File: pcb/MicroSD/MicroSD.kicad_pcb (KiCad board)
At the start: 2 copper layers, 30 x 40 mm, 15 parts, among them J1 Micro_SD_Card, J2 Conn_01x06_MountingPin, U2 AMS1117, U3 74LVC125

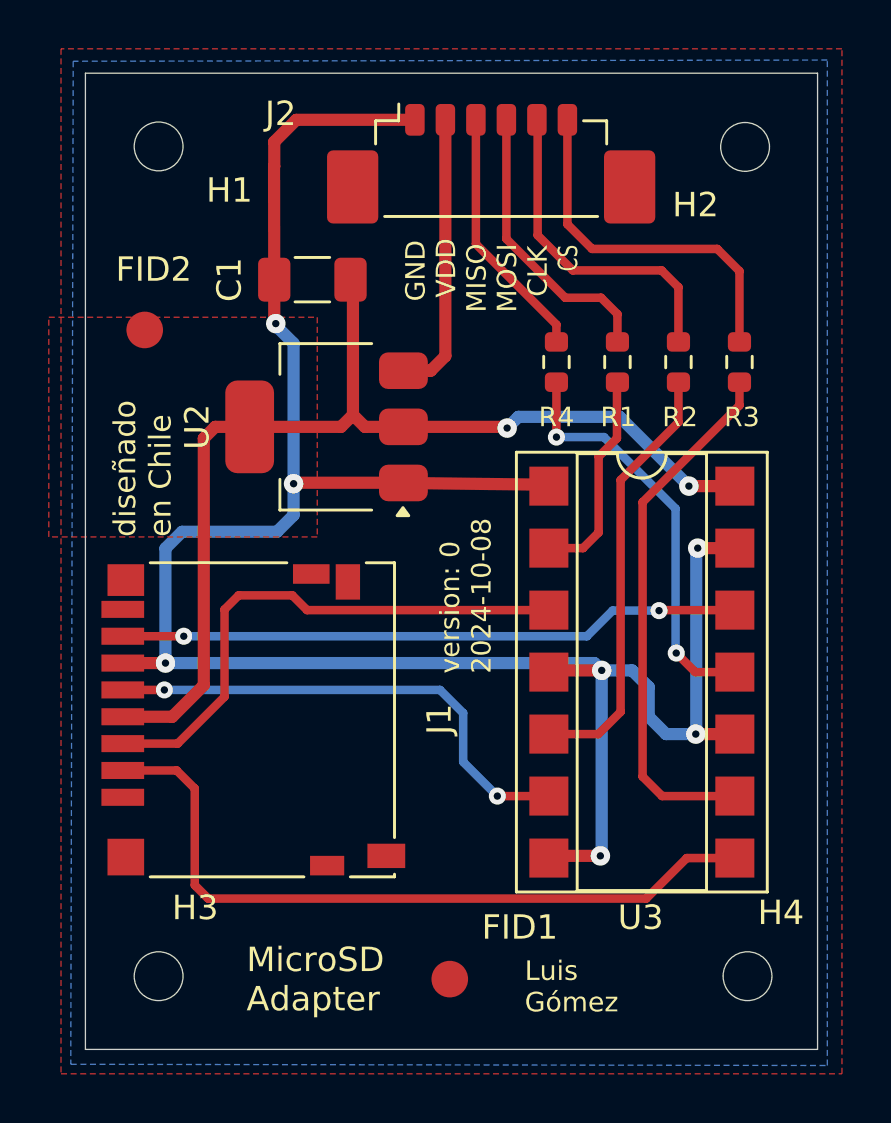
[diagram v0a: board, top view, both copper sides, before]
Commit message: se eliminan error del pcb
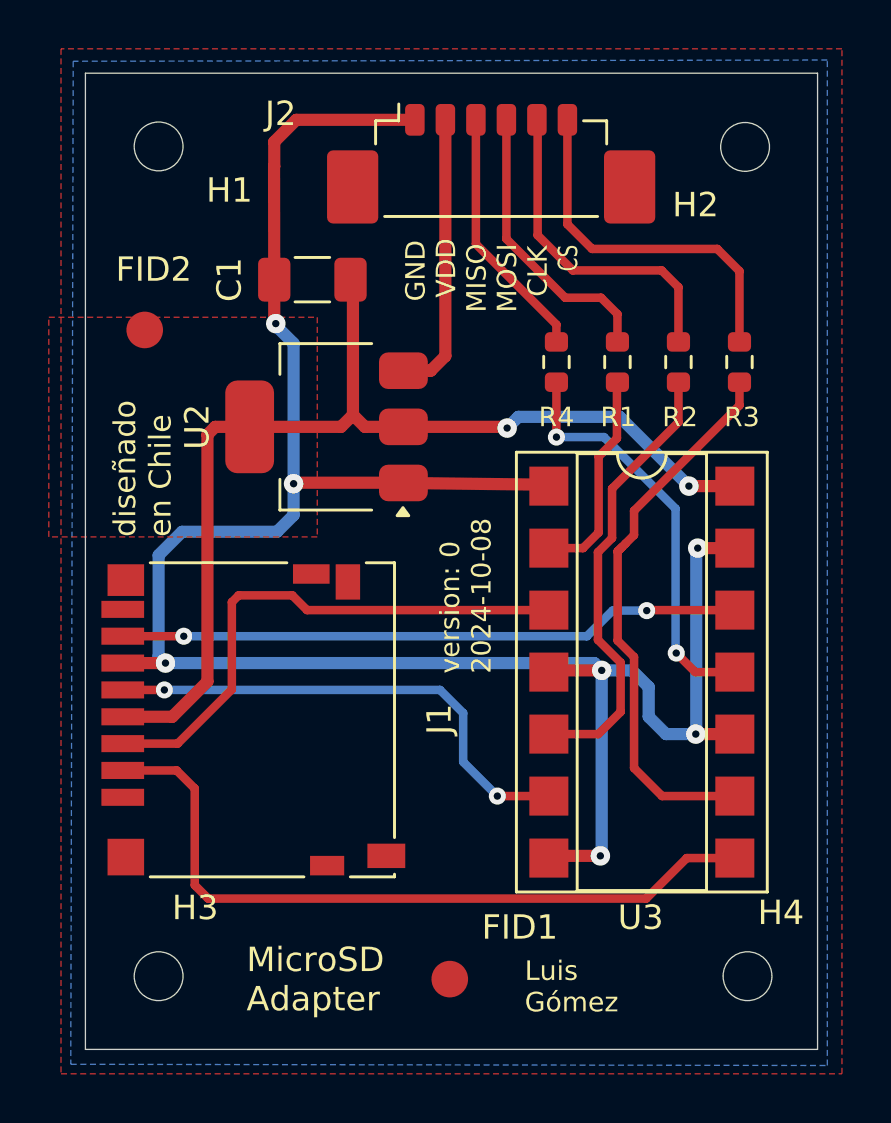
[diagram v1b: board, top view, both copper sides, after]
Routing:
- net Net-(R3-Pad2): track 21.9 -> 23.0 mm
- net Net-(R2-Pad2): track 17.8 -> 18.6 mm
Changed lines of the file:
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@@
+	)
+	(segment
+		(start 103.96 118.79)
+		(end 103 119.75)
+		(width 0.5)
+		(layer "B.Cu")
+		(net 1)
 	)
 	(segment
@@
 	)
 	(segment
+		(start 103 119.75)
+		(end 103 123.89)
+		(width 0.5)
+		(layer "B.Cu")
+		(net 1)
+	)
+	(segment
+		(start 125.01 127.08)
+		(end 123.79 127.08)
+		(width 0.5)
+		(layer "B.Cu")
+		(net 1)
+	)
+	(segment
+		(start 107.8 110.34)
+		(end 107.8 110.26)
+		(width 0.5)
+		(layer "B.Cu")
+		(net 1)
+	)
+	(segment
+		(start 107.85 118.79)
+		(end 103.96 118.79)
+		(width 0.5)
+		(layer "B.Cu")
+		(net 1)
+	)
+	(segment
+		(start 125.01 127.08)
+		(end 125.03 127.06)
+		(width 0.5)
+		(layer "B.Cu")
+		(net 1)
+	)
+	(segment
+		(start 125.03 119.52)
+		(end 125.09 119.46)
+		(width 0.5)
+		(layer "B.Cu")
+		(net 1)
+	)
+	(segment
+		(start 121.155 132.015)
+		(end 121.155 124.47)
+		(width 0.5)
+		(layer "B.Cu")
+		(net 1)
+	)
+	(segment
+		(start 123.08 125.15)
+		(end 122.4 124.47)
+		(width 0.5)
+		(layer "B.Cu")
+		(net 1)
+	)
+	(segment
+		(start 103 123.89)
+		(end 103.28 124.17)
+		(width 0.5)
+		(layer "B.Cu")
+		(net 1)
+	)
+	(segment
+		(start 108.53 111.07)
+		(end 107.8 110.34)
+		(width 0.5)
+		(layer "B.Cu")
+		(net 1)
+	)
+	(segment
 		(start 108.53 118.11)
 		(end 107.85 118.79)
@@
 	)
 	(segment
-		(start 125.01 127.08)
-		(end 123.79 127.08)
-		(width 0.5)
-		(layer "B.Cu")
-		(net 1)
-	)
-	(segment
-		(start 107.8 110.34)
-		(end 107.8 110.26)
-		(width 0.5)
-		(layer "B.Cu")
-		(net 1)
-	)
-	(segment
-		(start 125.01 127.08)
-		(end 125.03 127.06)
-		(width 0.5)
-		(layer "B.Cu")
-		(net 1)
-	)
-	(segment
-		(start 103.96 118.79)
-		(end 103.28 119.47)
-		(width 0.5)
-		(layer "B.Cu")
-		(net 1)
-	)
-	(segment
-		(start 125.03 119.52)
-		(end 125.09 119.46)
-		(width 0.5)
-		(layer "B.Cu")
-		(net 1)
-	)
-	(segment
-		(start 121.155 132.015)
-		(end 121.155 124.47)
-		(width 0.5)
-		(layer "B.Cu")
-		(net 1)
-	)
-	(segment
-		(start 123.08 125.15)
-		(end 122.4 124.47)
-		(width 0.5)
-		(layer "B.Cu")
-		(net 1)
-	)
-	(segment
 		(start 108.53 116.82)
 		(end 108.53 118.11)
-		(width 0.5)
-		(layer "B.Cu")
-		(net 1)
-	)
-	(segment
-		(start 108.53 111.07)
-		(end 107.8 110.34)
-		(width 0.5)
-		(layer "B.Cu")
-		(net 1)
-	)
-	(segment
-		(start 107.85 118.79)
-		(end 103.96 118.79)
-		(width 0.5)
-		(layer "B.Cu")
-		(net 1)
-	)
-	(segment
-		(start 103.28 119.47)
-		(end 103.28 124.17)
 		(width 0.5)
 		(layer "B.Cu")
@@
 	)
 	(segment
+		(start 106 121.675)
+		(end 106 125.25)
+		(width 0.35)
+		(layer "F.Cu")
+		(net 5)
+	)
+	(segment
+		(start 103.78 127.47)
+		(end 101.53 127.47)
+		(width 0.35)
+		(layer "F.Cu")
+		(net 5)
+	)
+	(segment
 		(start 106.28 121.395)
-		(end 105.7 121.975)
+		(end 106 121.675)
+		(width 0.35)
+		(layer "F.Cu")
+		(net 5)
+	)
+	(segment
+		(start 109.082488 122)
+		(end 108.477488 121.395)
 		(width 0.35)
 		(layer "F.Cu")
@@
 	)
 	(segment
-		(start 105.7 125.55)
+		(start 106 125.25)
 		(end 103.78 127.47)
 		(width 0.35)
@@
 	)
 	(segment
-		(start 109.082488 122)
-		(end 108.477488 121.395)
-		(width 0.35)
-		(layer "F.Cu")
-		(net 5)
-	)
-	(segment
-		(start 105.7 121.975)
-		(end 105.7 125.55)
-		(width 0.35)
-		(layer "F.Cu")
-		(net 5)
-	)
-	(segment
-		(start 103.78 127.47)
-		(end 101.53 127.47)
-		(width 0.35)
-		(layer "F.Cu")
-		(net 5)
-	)
-	(segment
-		(start 123.505 122.02)
-		(end 123.525 122)
+		(start 123.02 122)
+		(end 126.61 122)
 		(width 0.35)
 		(layer "F.Cu")
@@
 	)
 	(segment
-		(start 123.525 122)
-		(end 126.61 122)
+		(start 123 122.02)
+		(end 123.02 122)
 		(width 0.35)
 		(layer "F.Cu")
@@
 	)
 	(via
-		(at 123.505 122.02)
+		(at 123 122.02)
 		(size 0.7)
 		(drill 0.3)
@@
 	)
 	(segment
+		(start 123 122.02)
+		(end 121.6 122.02)
+		(width 0.35)
+		(layer "B.Cu")
+		(net 6)
+	)
+	(segment
+		(start 121.6 122.02)
+		(end 120.55 123.07)
+		(width 0.35)
+		(layer "B.Cu")
+		(net 6)
+	)
+	(segment
 		(start 120.55 123.07)
 		(end 104.03 123.07)
@@
 	)
 	(segment
-		(start 123.505 122.02)
-		(end 121.6 122.02)
-		(width 0.35)
-		(layer "B.Cu")
-		(net 6)
-	)
-	(segment
-		(start 121.6 122.02)
-		(end 120.55 123.07)
-		(width 0.35)
-		(layer "B.Cu")
-		(net 6)
-	)
-	(segment
 		(start 126.8 111.01)
 		(end 126.8 108.11)
@@
 	)
 	(segment
-		(start 121.93 116.67)
-		(end 121.93 126.17)
+		(start 121 123.218984)
+		(end 121.93 124.148984)
+		(width 0.35)
+		(layer "F.Cu")
+		(net 15)
+	)
+	(segment
+		(start 121 119.627818)
+		(end 121 123.218984)
 		(width 0.35)
 		(layer "F.Cu")
@@
 	)
 	(segment
+		(start 124.3 114.3)
+		(end 121.58 117.02)
+		(width 0.35)
+		(layer "F.Cu")
+		(net 15)
+	)
+	(segment
+		(start 121.58 119.047818)
+		(end 121 119.627818)
+		(width 0.35)
+		(layer "F.Cu")
+		(net 15)
+	)
+	(segment
+		(start 121.58 117.02)
+		(end 121.58 119.047818)
+		(width 0.35)
+		(layer "F.Cu")
+		(net 15)
+	)
+	(segment
+		(start 121.02 127.08)
+		(end 118.99 127.08)
+		(width 0.35)
+		(layer "F.Cu")
+		(net 15)
+	)
+	(segment
 		(start 124.3 112.66)
 		(end 124.3 114.3)
@@
 	)
 	(segment
-		(start 124.3 114.3)
-		(end 121.93 116.67)
+		(start 121.93 124.148984)
+		(end 121.93 126.17)
 		(width 0.35)
 		(layer "F.Cu")
 		(net 15)
-	)
-	(segment
-		(start 121.02 127.08)
-		(end 118.99 127.08)
-		(width 0.35)
-		(layer "F.Cu")
-		(net 15)
-	)
-	(segment
-		(start 126.8 113.61)
-		(end 122.83 117.58)
-		(width 0.35)
-		(layer "F.Cu")
-		(net 16)
 	)
 	(segment
@@
 	)
 	(segment
-		(start 122.83 128.82)
+		(start 122.48 128.47)
 		(end 123.63 129.62)
-		(width 0.35)
-		(layer "F.Cu")
-		(net 16)
-	)
-	(segment
-		(start 122.83 117.58)
-		(end 122.83 128.82)
 		(width 0.35)
 		(layer "F.Cu")
@@
 		(start 123.63 129.62)
 		(end 126.61 129.62)
+		(width 0.35)
+		(layer "F.Cu")
+		(net 16)
+	)
+	(segment
+		(start 126.8 113.61)
+		(end 122.48 117.93)
+		(width 0.35)
+		(layer "F.Cu")
+		(net 16)
+	)
+	(segment
+		(start 122.48 118.925636)
+		(end 122.13 119.275636)
+		(width 0.35)
+		(layer "F.Cu")
+		(net 16)
+	)
+	(segment
+		(start 122.48 123.921166)
+		(end 122.48 128.47)
+		(width 0.35)
+		(layer "F.Cu")
+		(net 16)
+	)
+	(segment
+		(start 122.48 117.93)
+		(end 122.48 118.925636)
+		(width 0.35)
+		(layer "F.Cu")
+		(net 16)
+	)
+	(segment
+		(start 121.807817 119.597818)
+		(end 121.999999 119.405636)
+		(width 0.35)
+		(layer "F.Cu")
+		(net 16)
+	)
+	(segment
+		(start 122.13 119.275636)
+		(end 121.807817 119.597818)
+		(width 0.35)
+		(layer "F.Cu")
+		(net 16)
+	)
+	(segment
+		(start 121.807817 123.248983)
+		(end 122.48 123.921166)
+		(width 0.35)
+		(layer "F.Cu")
+		(net 16)
+	)
+	(segment
+		(start 121.807817 119.597818)
+		(end 121.807817 123.248983)
 		(width 0.35)
 		(layer "F.Cu")
@@
 	)
 	(segment
-		(start 104.85 125.08)
-		(end 104.85 114.96)
+		(start 105 114.81)
+		(end 105.32 114.49)
 		(width 0.5)
 		(layer "F.Cu")
@@
 	)
 	(segment
-		(start 104.85 114.96)
-		(end 105.32 114.49)
+		(start 105.32 114.49)
+		(end 106.73 114.49)
 		(width 0.5)
 		(layer "F.Cu")
@@
 	(segment
 		(start 103.56 126.37)
-		(end 104.85 125.08)
+		(end 105 124.93)
 		(width 0.5)
 		(layer "F.Cu")
@@
 	)
 	(segment
-		(start 105.32 114.49)
-		(end 106.73 114.49)
-		(width 0.5)
-		(layer "F.Cu")
+		(start 105 124.93)
+		(end 105 114.81)
+		(width 0.5)
+		(layer "F.Cu")
